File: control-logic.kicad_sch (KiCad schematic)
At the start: 3 parts, among them SW1 Button, U41 74HCT00

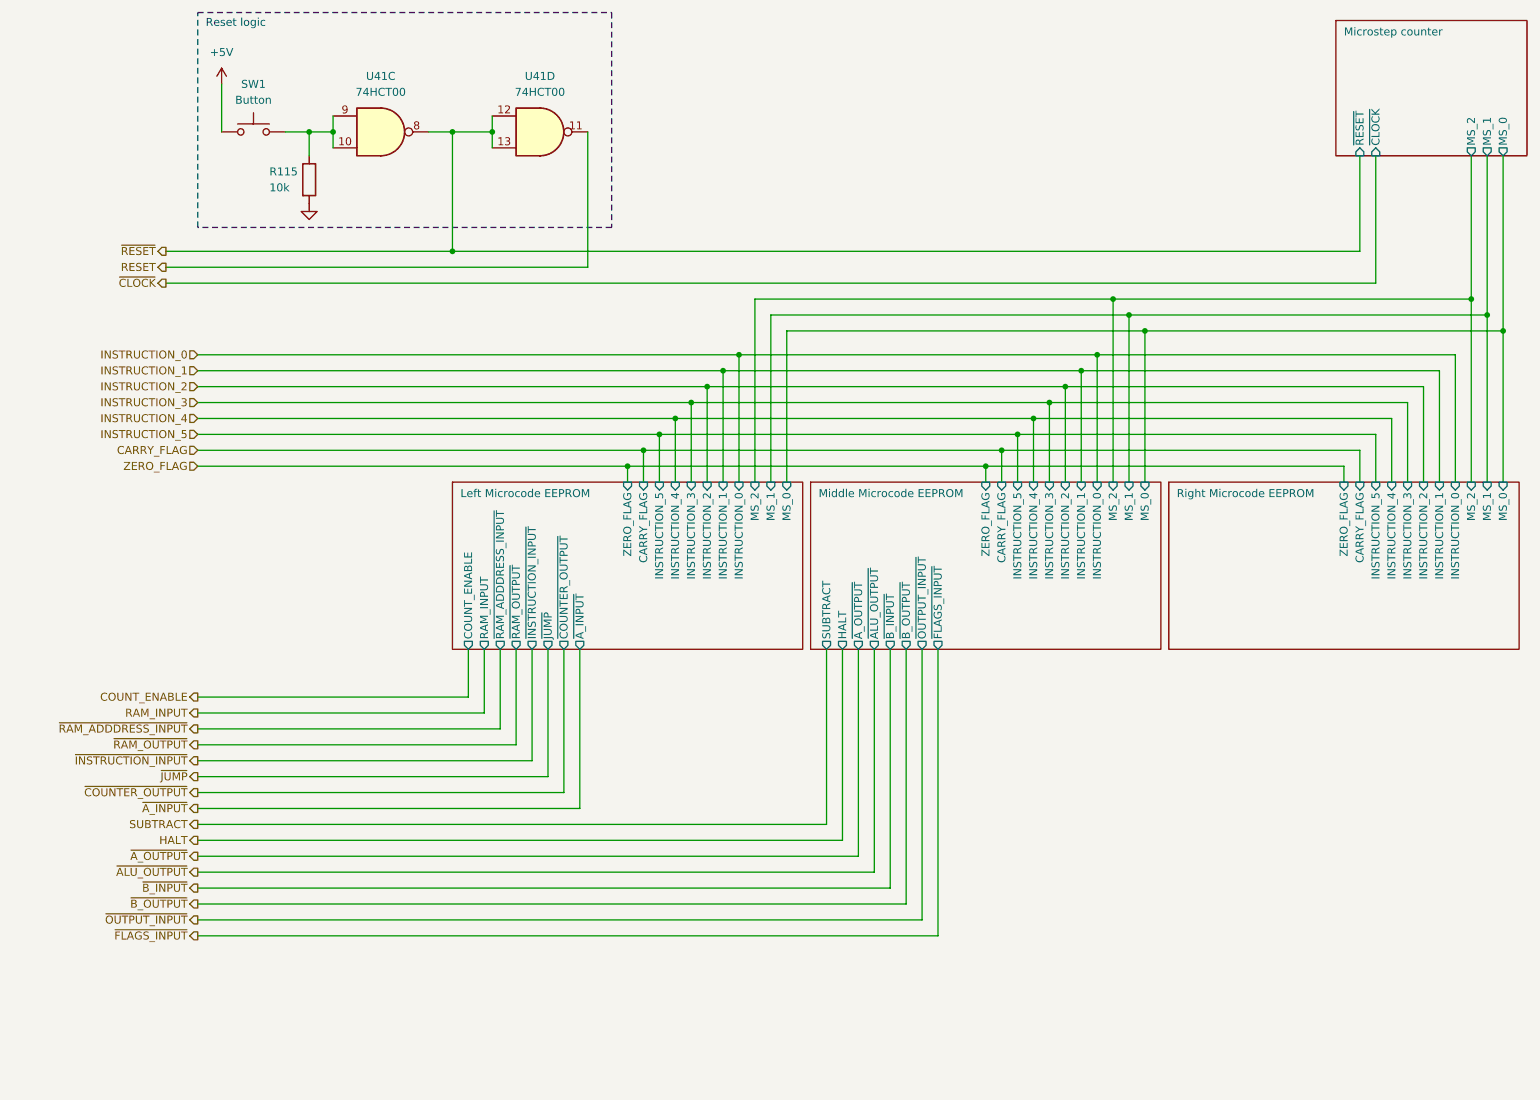
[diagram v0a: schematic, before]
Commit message: added stack and x register.  Added logic for stack_address so ram address 7 gets passes and ram address 8 is high
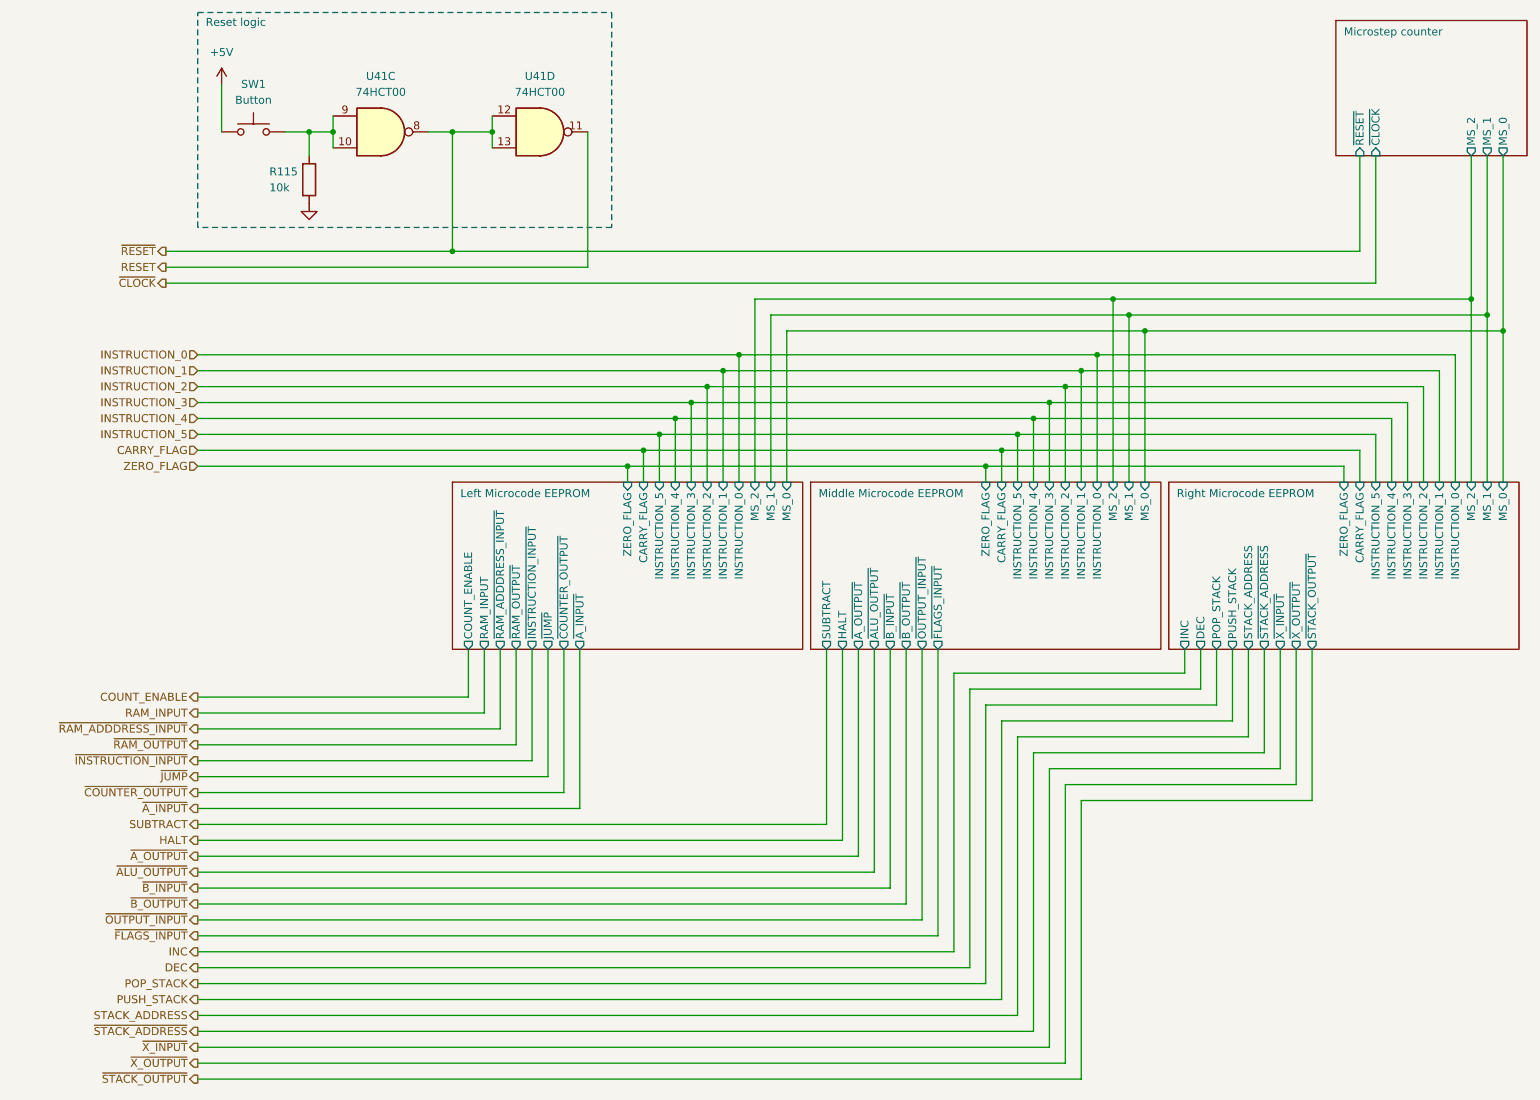
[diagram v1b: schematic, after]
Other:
- sheet Right Microcode EEPROM ports: added DEC, INC, POP_STACK, PUSH_STACK, STACK_ADDRESS, ~{STACK_ADDRESS}, ~{STACK_OUTPUT}, ~{X_INPUT}, ~{X_OUTPUT}; removed none

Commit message: some cleanup
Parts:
- renumbered R115 to R116
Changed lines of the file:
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@@
   (symbol (lib_id "power:GND") (at 52.07 49.53 0) (unit 1)
     (in_bom yes) (on_board yes) (dnp no) (fields_autoplaced)
-    (property "Reference" "#PWR0173" (at 52.07 55.88 0)
+    (property "Reference" "#PWR0168" (at 52.07 55.88 0)
       (effects (font (size 1.27 1.27)) hide)
     )
@@
       (project "8-bit-cpu"
         (path "/100bb8d1-c3d6-4e1f-87b6-72e4e187243c/cbe1ebf3-0fd2-468b-b752-73c1c63eb76e"
-          (reference "#PWR0173") (unit 1)
+          (reference "#PWR0168") (unit 1)
         )
       )
@@
   (symbol (lib_id "power:+5V") (at 38.1 30.48 0) (unit 1)
     (in_bom yes) (on_board yes) (dnp no) (fields_autoplaced)
-    (property "Reference" "#PWR0170" (at 38.1 34.29 0)
+    (property "Reference" "#PWR0167" (at 38.1 34.29 0)
       (effects (font (size 1.27 1.27)) hide)
     )
@@
       (project "8-bit-cpu"
         (path "/100bb8d1-c3d6-4e1f-87b6-72e4e187243c/cbe1ebf3-0fd2-468b-b752-73c1c63eb76e"
-          (reference "#PWR0170") (unit 1)
+          (reference "#PWR0167") (unit 1)
         )
       )
@@
   (symbol (lib_id "Device:R") (at 52.07 45.72 0) (unit 1)
     (in_bom yes) (on_board yes) (dnp no)
-    (property "Reference" "R115" (at 45.72 44.45 0)
+    (property "Reference" "R116" (at 45.72 44.45 0)
       (effects (font (size 1.27 1.27)) (justify left))
     )
@@
       (project "8-bit-cpu"
         (path "/100bb8d1-c3d6-4e1f-87b6-72e4e187243c/cbe1ebf3-0fd2-468b-b752-73c1c63eb76e"
-          (reference "R115") (unit 1)
+          (reference "R116") (unit 1)
         )
       )

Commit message: add arduino headers for programming
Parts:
- R116: footprint (none) -> Resistor_THT:R_Axial_DIN0204_L3.6mm_D1.6mm_P7.62mm_Horizontal
- U41: footprint (none) -> Package_DIP:DIP-14_W7.62mm
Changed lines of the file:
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@@
       (effects (font (size 1.27 1.27)))
     )
-    (property "Footprint" "" (at 88.9 38.1 0)
+    (property "Footprint" "Package_DIP:DIP-14_W7.62mm" (at 88.9 38.1 0)
       (effects (font (size 1.27 1.27)) hide)
     )
@@
       (effects (font (size 1.27 1.27)))
     )
-    (property "Footprint" "" (at 63.5 38.1 0)
+    (property "Footprint" "Package_DIP:DIP-14_W7.62mm" (at 63.5 38.1 0)
       (effects (font (size 1.27 1.27)) hide)
     )
@@
       (effects (font (size 1.27 1.27)) (justify left))
     )
-    (property "Footprint" "" (at 50.292 45.72 90)
+    (property "Footprint" "Resistor_THT:R_Axial_DIN0204_L3.6mm_D1.6mm_P7.62mm_Horizontal" (at 50.292 45.72 90)
       (effects (font (size 1.27 1.27)) hide)
     )

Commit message: trying to solve issues
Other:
- added sheet EEPROM address buffer (eeprom-address-buffer.kicad_sch)
- sheet Left Microcode EEPROM ports: added EEPROM_10, EEPROM_3, EEPROM_4, EEPROM_5, EEPROM_6, EEPROM_7, EEPROM_8, EEPROM_9; removed CARRY_FLAG, INSTRUCTION_0, INSTRUCTION_1, INSTRUCTION_2, INSTRUCTION_3, INSTRUCTION_4, INSTRUCTION_5, ZERO_FLAG
- sheet Middle Microcode EEPROM ports: added EEPROM_10, EEPROM_3, EEPROM_4, EEPROM_5, EEPROM_6, EEPROM_7, EEPROM_8, EEPROM_9; removed CARRY_FLAG, INSTRUCTION_0, INSTRUCTION_1, INSTRUCTION_2, INSTRUCTION_3, INSTRUCTION_4, INSTRUCTION_5, ZERO_FLAG
- sheet Right Microcode EEPROM ports: added EEPROM_10, EEPROM_3, EEPROM_4, EEPROM_5, EEPROM_6, EEPROM_7, EEPROM_8, EEPROM_9, X_INPUT; removed CARRY_FLAG, INSTRUCTION_0, INSTRUCTION_1, INSTRUCTION_2, INSTRUCTION_3, INSTRUCTION_4, INSTRUCTION_5, ZERO_FLAG, ~{X_INPUT}

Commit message: cleanup
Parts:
- renumbered R116 to R115
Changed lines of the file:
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@@
   (symbol (lib_id "power:GND") (at 52.07 49.53 0) (unit 1)
     (in_bom yes) (on_board yes) (dnp no) (fields_autoplaced)
-    (property "Reference" "#PWR0172" (at 52.07 55.88 0)
+    (property "Reference" "#PWR0171" (at 52.07 55.88 0)
       (effects (font (size 1.27 1.27)) hide)
     )
@@
       (project "8-bit-cpu"
         (path "/100bb8d1-c3d6-4e1f-87b6-72e4e187243c/cbe1ebf3-0fd2-468b-b752-73c1c63eb76e"
-          (reference "#PWR0172") (unit 1)
+          (reference "#PWR0171") (unit 1)
         )
       )
@@
   (symbol (lib_id "power:+5V") (at 38.1 30.48 0) (unit 1)
     (in_bom yes) (on_board yes) (dnp no) (fields_autoplaced)
-    (property "Reference" "#PWR0171" (at 38.1 34.29 0)
+    (property "Reference" "#PWR0170" (at 38.1 34.29 0)
       (effects (font (size 1.27 1.27)) hide)
     )
@@
       (project "8-bit-cpu"
         (path "/100bb8d1-c3d6-4e1f-87b6-72e4e187243c/cbe1ebf3-0fd2-468b-b752-73c1c63eb76e"
-          (reference "#PWR0171") (unit 1)
+          (reference "#PWR0170") (unit 1)
         )
       )
@@
   (symbol (lib_id "Device:R") (at 52.07 45.72 0) (unit 1)
     (in_bom yes) (on_board yes) (dnp no)
-    (property "Reference" "R116" (at 45.72 44.45 0)
+    (property "Reference" "R115" (at 45.72 44.45 0)
       (effects (font (size 1.27 1.27)) (justify left))
     )
@@
       (project "8-bit-cpu"
         (path "/100bb8d1-c3d6-4e1f-87b6-72e4e187243c/cbe1ebf3-0fd2-468b-b752-73c1c63eb76e"
-          (reference "R116") (unit 1)
+          (reference "R115") (unit 1)
         )
       )
